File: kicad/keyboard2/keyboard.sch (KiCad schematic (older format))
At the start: 140 parts, among them K0 KEYSW, K1 KEYSW, K10 KEYSW, K11 KEYSW, K12 KEYSW, K13 KEYSW, K14 KEYSW, K15 KEYSW, K16 KEYSW, K17 KEYSW, K18 KEYSW, K19 KEYSW, K2 KEYSW, K20 KEYSW, K21 KEYSW, K22 KEYSW, K23 KEYSW, K24 KEYSW, K25 KEYSW, K26 KEYSW, K27 KEYSW, K28 KEYSW, K29 KEYSW, K3 KEYSW, K30 KEYSW, K31 KEYSW, K32 KEYSW, K33 KEYSW, K34 KEYSW, K35 KEYSW, K36 KEYSW, K37 KEYSW, K38 KEYSW, K39 KEYSW, K4 KEYSW, K40 KEYSW, K41 KEYSW, K42 KEYSW, K43 KEYSW, K44 KEYSW, K45 KEYSW, K46 KEYSW, K47 KEYSW, K48 KEYSW, K49 KEYSW, K5 KEYSW, K50 KEYSW, K51 KEYSW, K52 KEYSW, K53 KEYSW, K54 KEYSW, K55 KEYSW, K56 KEYSW, K57 KEYSW, K58 KEYSW, K59 KEYSW, K6 KEYSW, K60 KEYSW, K61 KEYSW, K62 KEYSW, K63 KEYSW, K64 KEYSW, K65 KEYSW, K7 KEYSW, K9 KEYSW, U0 ATmega32U4-AU, Y0 16 MHZ

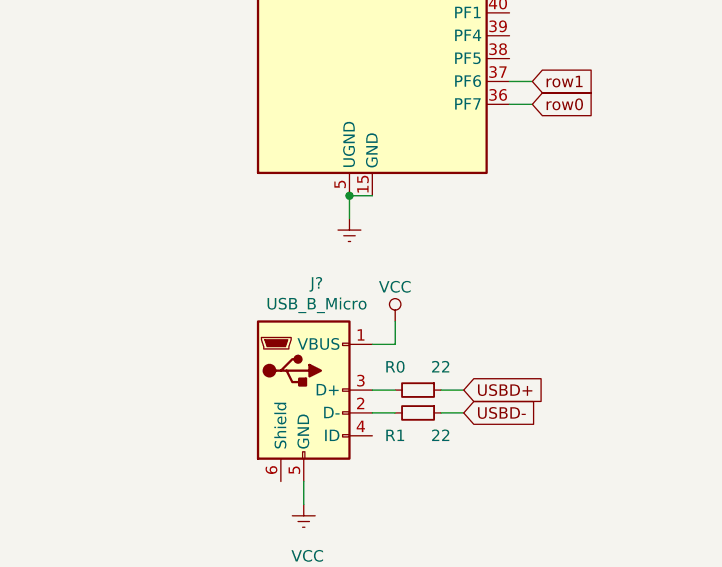
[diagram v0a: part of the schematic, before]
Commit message: completed main layout
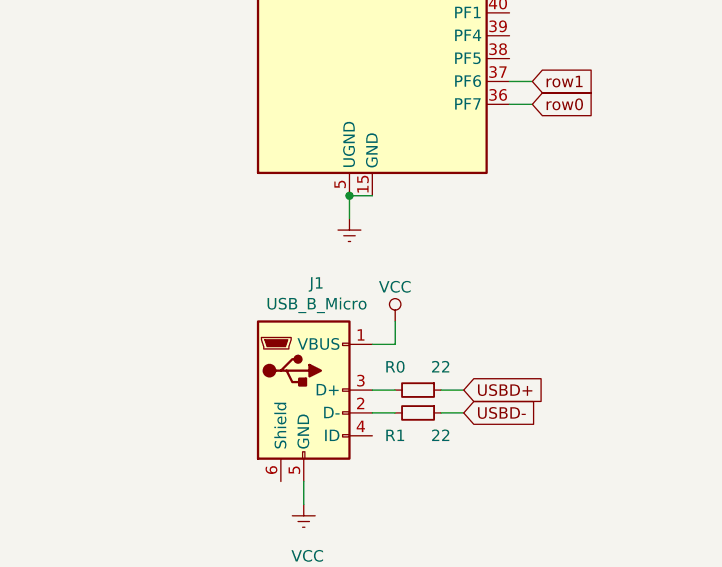
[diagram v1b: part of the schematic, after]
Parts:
- C0, C1, C2: footprint (none) -> Capacitor_SMD:C_1206_3216Metric_Pad1.42x1.75mm_HandSolder
- J1: renamed from J?; footprint (none) -> keyboard_parts:USB_microB
- JP0: footprint (none) -> Button_Switch_THT:SW_DIP_SPSTx01_Slide_6.7x4.1mm_W7.62mm_P2.54mm_LowProfile
- R0, R1, R2: footprint (none) -> Resistor_SMD:R_1206_3216Metric_Pad1.42x1.75mm_HandSolder
- Y0: footprint (none) -> Crystal:Crystal_SMD_Abracon_ABM3-2Pin_5.0x3.2mm_HandSoldering
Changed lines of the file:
@@
 	12750 11250 12750 11300
 $Comp
-L power:VCC #PWR?
+L power:VCC #PWR0101
 U 1 1 5E877798
 P 8850 3450
-F 0 "#PWR?" H 8850 3300 50  0001 C CNN
+F 0 "#PWR0101" H 8850 3300 50  0001 C CNN
 F 1 "VCC" H 8750 3450 50  0000 C CNN
 F 2 "" H 8850 3450 50  0001 C CNN
@@
 F 0 "Y0" V 8750 3000 50  0000 R CNN
 F 1 "16 MHZ" V 8350 3100 50  0000 R CNN
-F 2 "" H 8550 2950 50  0001 C CNN
+F 2 "Crystal:Crystal_SMD_Abracon_ABM3-2Pin_5.0x3.2mm_HandSoldering" H 8550 2950 50  0001 C CNN
 F 3 "~" H 8550 2950 50  0001 C CNN
 	1    8550 2950
@@
 F 0 "C0" V 8300 2750 50  0000 C CNN
 F 1 "22pf" V 8100 2850 50  0000 C CNN
-F 2 "" H 8288 2700 50  0001 C CNN
+F 2 "Capacitor_SMD:C_1206_3216Metric_Pad1.42x1.75mm_HandSolder" H 8288 2700 50  0001 C CNN
 F 3 "~" H 8250 2850 50  0001 C CNN
 	1    8250 2850
@@
 F 0 "C1" V 8200 2950 50  0000 C CNN
 F 1 "22pf" V 8400 3050 50  0000 C CNN
-F 2 "" H 8288 2900 50  0001 C CNN
+F 2 "Capacitor_SMD:C_1206_3216Metric_Pad1.42x1.75mm_HandSolder" H 8288 2900 50  0001 C CNN
 F 3 "~" H 8250 3050 50  0001 C CNN
 	1    8250 3050
@@
 	8550 3050 8400 3050
 $Comp
-L power:Earth #PWR?
+L power:Earth #PWR0102
 U 1 1 5E8F6444
 P 8000 3150
-F 0 "#PWR?" H 8000 2900 50  0001 C CNN
+F 0 "#PWR0102" H 8000 2900 50  0001 C CNN
 F 1 "Earth" H 8000 3000 50  0001 C CNN
 F 2 "" H 8000 3150 50  0001 C CNN
@@
 F 0 "C2" V 8450 4050 50  0000 C CNN
 F 1 "1uf" V 8550 4050 50  0000 C CNN
-F 2 "" H 8538 3800 50  0001 C CNN
+F 2 "Capacitor_SMD:C_1206_3216Metric_Pad1.42x1.75mm_HandSolder" H 8538 3800 50  0001 C CNN
 F 3 "~" H 8500 3950 50  0001 C CNN
 	1    8500 3950
@@
 $EndComp
 $Comp
-L power:Earth #PWR?
+L power:Earth #PWR0103
 U 1 1 5EA58D58
 P 9400 6050
-F 0 "#PWR?" H 9400 5800 50  0001 C CNN
+F 0 "#PWR0103" H 9400 5800 50  0001 C CNN
 F 1 "Earth" H 9400 5900 50  0001 C CNN
 F 2 "" H 9400 6050 50  0001 C CNN
@@
 	9400 5950 9400 6050
 $Comp
-L power:VCC #PWR?
+L power:VCC #PWR0104
 U 1 1 5EAC4B94
 P 9400 2300
-F 0 "#PWR?" H 9400 2150 50  0001 C CNN
+F 0 "#PWR0104" H 9400 2150 50  0001 C CNN
 F 1 "VCC" H 9300 2300 50  0000 C CNN
 F 2 "" H 9400 2300 50  0001 C CNN
@@
 col6
 $Comp
-L power:Earth #PWR?
+L power:Earth #PWR0105
 U 1 1 5F024DCA
 P 10450 4850
-F 0 "#PWR?" H 10450 4600 50  0001 C CNN
+F 0 "#PWR0105" H 10450 4600 50  0001 C CNN
 F 1 "Earth" H 10450 4700 50  0001 C CNN
 F 2 "" H 10450 4850 50  0001 C CNN
@@
 	8350 3950 8250 3950
 $Comp
-L power:Earth #PWR?
+L power:Earth #PWR0106
 U 1 1 5EA239E3
 P 8250 4050
-F 0 "#PWR?" H 8250 3800 50  0001 C CNN
+F 0 "#PWR0106" H 8250 3800 50  0001 C CNN
 F 1 "Earth" H 8250 3900 50  0001 C CNN
 F 2 "" H 8250 4050 50  0001 C CNN
@@
 $EndComp
 $Comp
-L power:Earth #PWR?
+L power:Earth #PWR0107
 U 1 1 5F5FBE56
 P 9200 7300
-F 0 "#PWR?" H 9200 7050 50  0001 C CNN
+F 0 "#PWR0107" H 9200 7050 50  0001 C CNN
 F 1 "Earth" H 9200 7150 50  0001 C CNN
 F 2 "" H 9200 7300 50  0001 C CNN
@@
 F 0 "R0" V 9600 6700 50  0000 C CNN
 F 1 "22" V 9600 6900 50  0000 C CNN
-F 2 "" H 9700 6800 50  0001 C CNN
+F 2 "Resistor_SMD:R_1206_3216Metric_Pad1.42x1.75mm_HandSolder" H 9700 6800 50  0001 C CNN
 F 3 "~" H 9700 6800 50  0001 C CNN
 	1    9700 6800
@@
 F 0 "R1" V 9800 6800 50  0000 C CNN
 F 1 "22" V 9800 7000 50  0000 C CNN
-F 2 "" H 9700 6900 50  0001 C CNN
+F 2 "Resistor_SMD:R_1206_3216Metric_Pad1.42x1.75mm_HandSolder" H 9700 6900 50  0001 C CNN
 F 3 "~" H 9700 6900 50  0001 C CNN
 	1    9700 6900
@@
 	9800 6900 9900 6900
 $Comp
-L power:VCC #PWR?
+L power:VCC #PWR0108
 U 1 1 5F7272AB
 P 9600 6500
-F 0 "#PWR?" H 9600 6350 50  0001 C CNN
+F 0 "#PWR0108" H 9600 6350 50  0001 C CNN
 F 1 "VCC" H 9600 6650 50  0000 C CNN
 F 2 "" H 9600 6500 50  0001 C CNN
@@
 	9600 6600 9600 6500
 $Comp
-L Connector:USB_B_Micro J?
+L Connector:USB_B_Micro J1
 U 1 1 5F7A153D
 P 9200 6800
-F 0 "J?" H 9257 7267 50  0000 C CNN
+F 0 "J1" H 9257 7267 50  0000 C CNN
 F 1 "USB_B_Micro" H 9257 7176 50  0000 C CNN
-F 2 "" H 9350 6750 50  0001 C CNN
+F 2 "keyboard_parts:USB_microB" H 9350 6750 50  0001 C CNN
 F 3 "~" H 9350 6750 50  0001 C CNN
 	1    9200 6800
@@
 F 0 "R2" H 9250 8000 50  0000 L CNN
 F 1 "10k" H 9250 7850 50  0000 L CNN
-F 2 "" H 9200 7900 50  0001 C CNN
+F 2 "Resistor_SMD:R_1206_3216Metric_Pad1.42x1.75mm_HandSolder" H 9200 7900 50  0001 C CNN
 F 3 "~" H 9200 7900 50  0001 C CNN
 	1    9200 7900
@@
 $EndComp
 $Comp
-L power:VCC #PWR?
+L power:VCC #PWR0109
 U 1 1 5FA638D0
 P 9200 7700
-F 0 "#PWR?" H 9200 7550 50  0001 C CNN
+F 0 "#PWR0109" H 9200 7550 50  0001 C CNN
 F 1 "VCC" H 9217 7873 50  0000 C CNN
 F 2 "" H 9200 7700 50  0001 C CNN
@@
 F 0 "JP0" H 9400 8050 50  0000 C CNN
 F 1 " " H 9400 8244 50  0000 C CNN
-F 2 "" H 9400 8150 50  0001 C CNN
+F 2 "Button_Switch_THT:SW_DIP_SPSTx01_Slide_6.7x4.1mm_W7.62mm_P2.54mm_LowProfile" H 9400 8150 50  0001 C CNN
 F 3 "~" H 9400 8150 50  0001 C CNN
 	1    9400 8150
@@
 Connection ~ 9200 8150
 $Comp
-L power:Earth #PWR?
+L power:Earth #PWR0110
 U 1 1 5FAE5CD6
 P 9600 8250
-F 0 "#PWR?" H 9600 8000 50  0001 C CNN
+F 0 "#PWR0110" H 9600 8000 50  0001 C CNN
 F 1 "Earth" H 9600 8100 50  0001 C CNN
 F 2 "" H 9600 8250 50  0001 C CNN

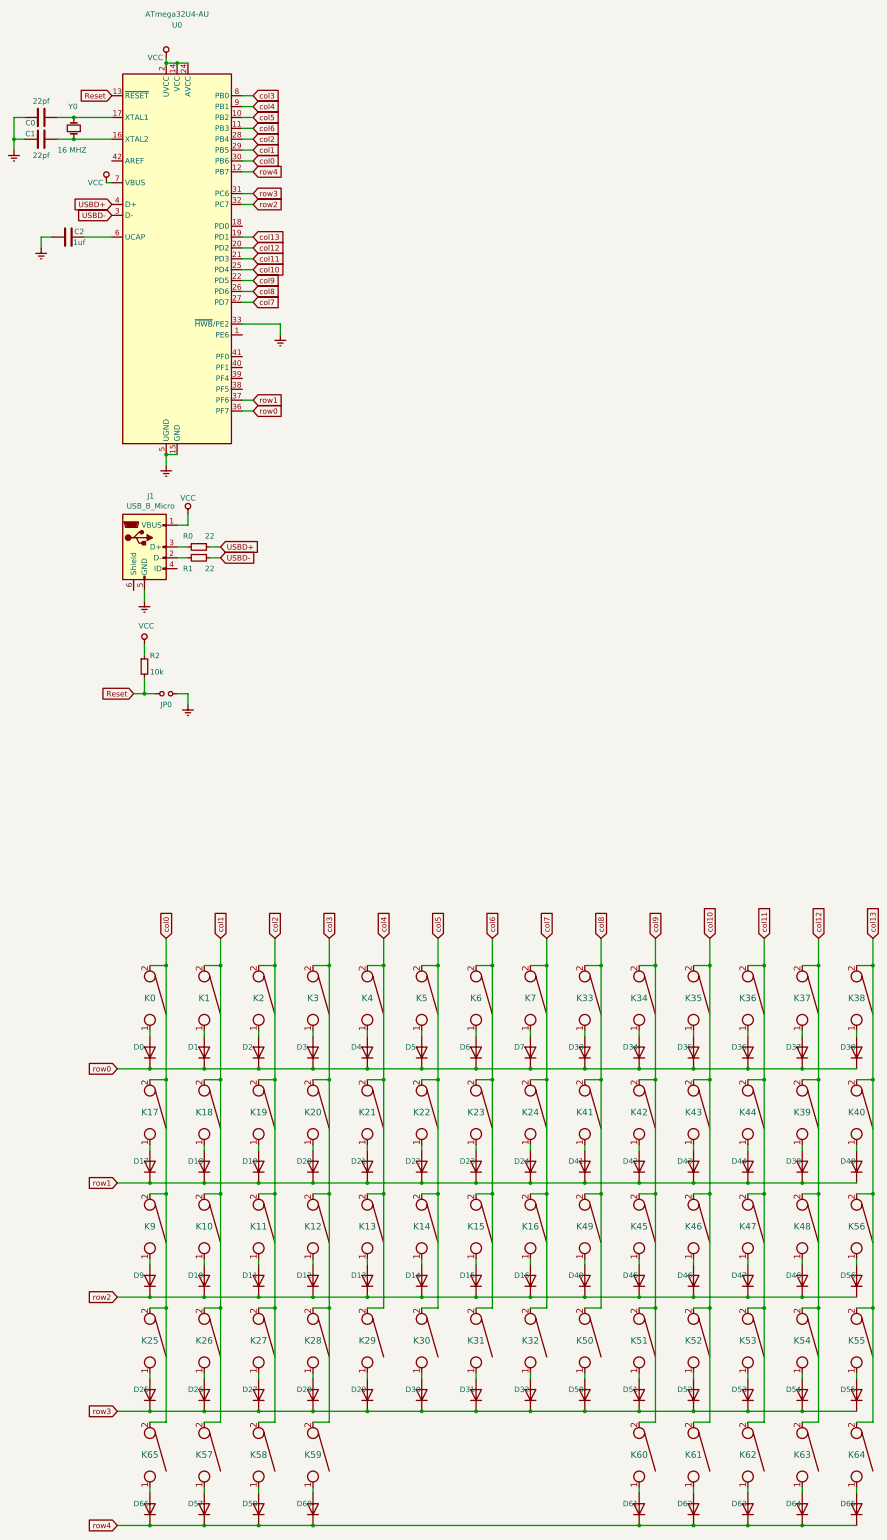
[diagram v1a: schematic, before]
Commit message: Completed first attempt at keyboard2 tracks
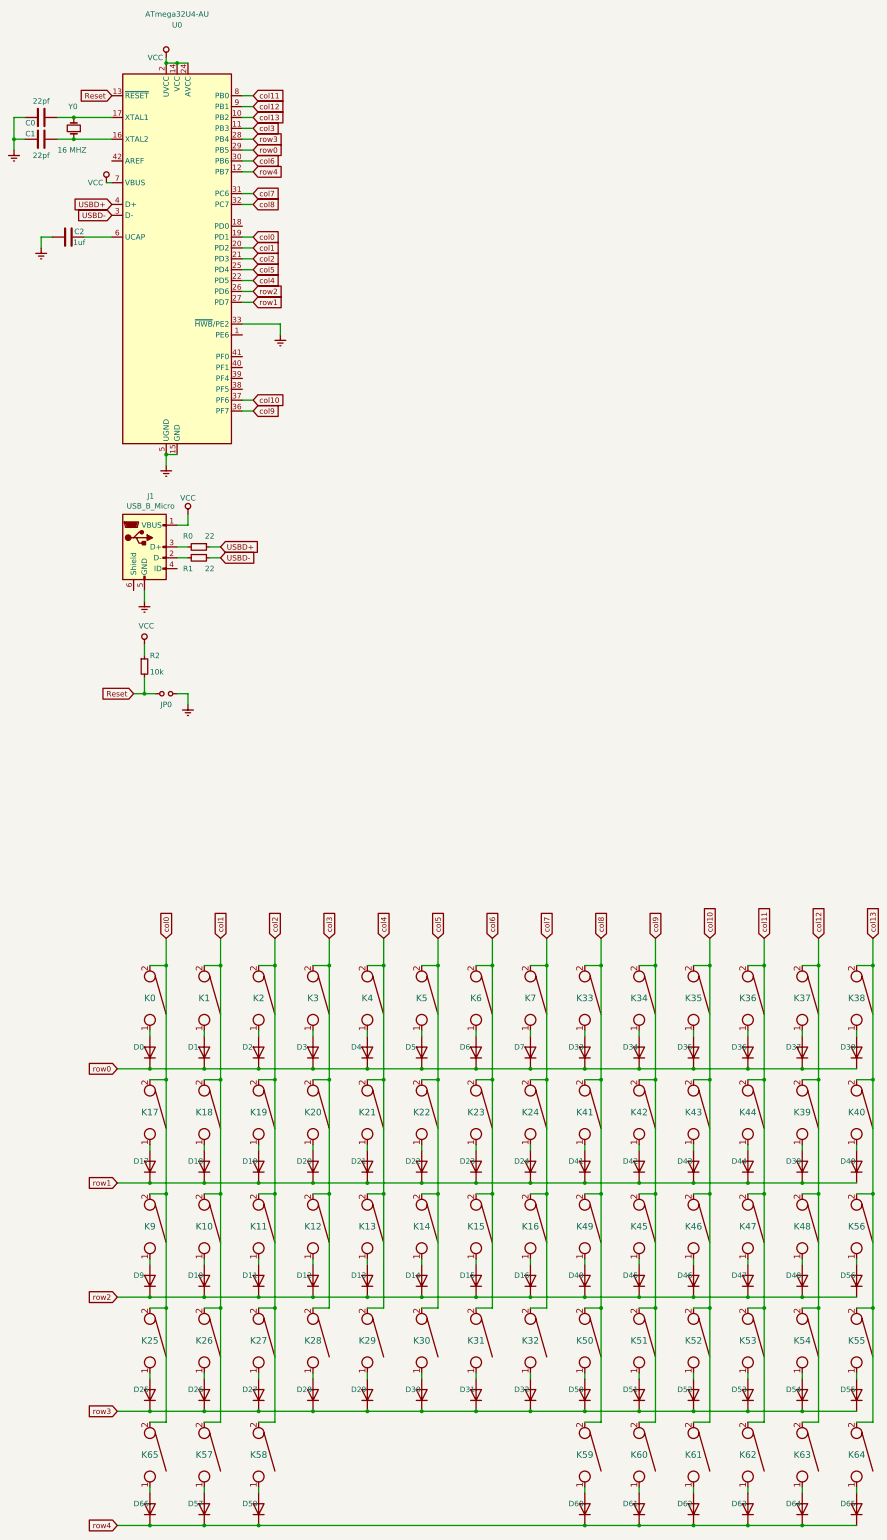
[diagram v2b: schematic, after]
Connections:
- net col0: now also U0.19 (PD1); no longer U0.30 (PB6)
- net col1: now also U0.20 (PD2); no longer U0.29 (PB5)
- net col10: now also U0.37 (PF6); no longer U0.25 (PD4)
- net col11: now also U0.8 (PB0); no longer U0.21 (PD3)
- net col12: now also U0.9 (PB1); no longer U0.20 (PD2)
- net col13: now also U0.10 (PB2); no longer U0.19 (PD1)
- net col2: now also U0.21 (PD3); no longer U0.28 (PB4)
- net col3: now also U0.11 (PB3); no longer K59.2, U0.8 (PB0)
- net col4: now also U0.22 (PD5); no longer U0.9 (PB1)
- net col5: now also U0.25 (PD4); no longer U0.10 (PB2)
- net col6: now also U0.30 (PB6); no longer U0.11 (PB3)
- net col7: now also U0.31 (PC6); no longer U0.27 (PD7)
- net col8: now also K59.2, U0.32 (PC7); no longer U0.26 (PD6)
- net col9: now also U0.36 (PF7); no longer U0.22 (PD5)
- net row0: now also U0.29 (PB5); no longer U0.36 (PF7)
- net row1: now also U0.27 (PD7); no longer U0.37 (PF6)
- net row2: now also U0.26 (PD6); no longer U0.32 (PC7)
- net row3: now also U0.28 (PB4); no longer U0.31 (PC6)
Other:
- moved on the sheet: D60, K59
